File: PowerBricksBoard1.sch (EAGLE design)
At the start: 9 parts

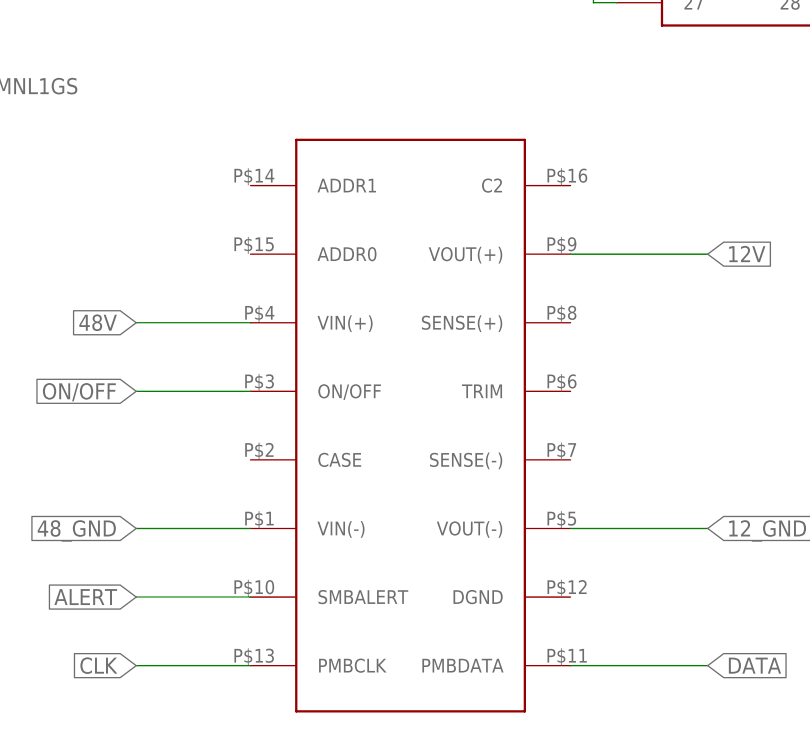
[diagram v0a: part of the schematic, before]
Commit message: updated brick part and edited connetors
had to move connector for capacitor placement
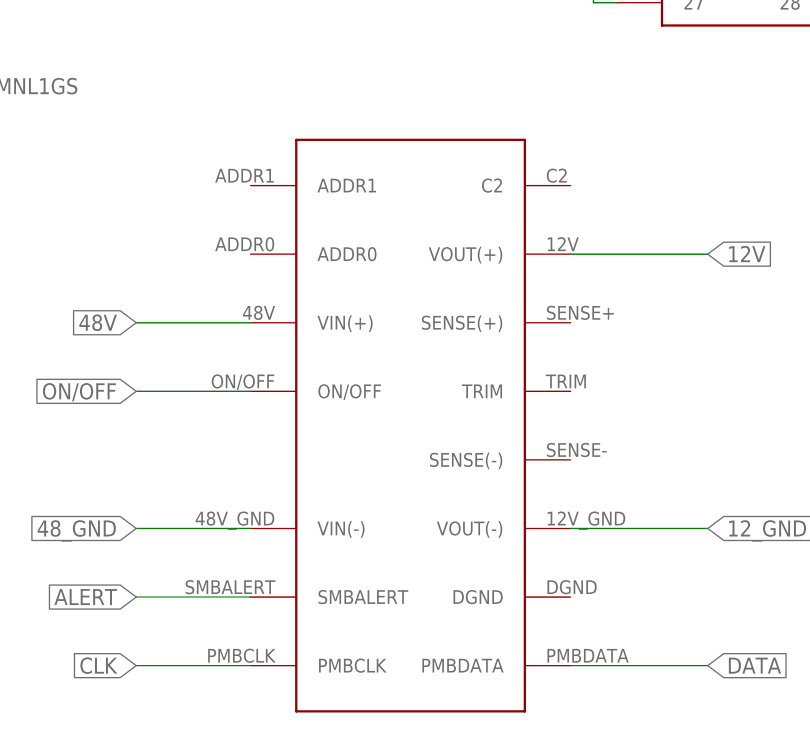
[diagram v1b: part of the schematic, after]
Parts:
- U$5: device Brickboard_Connector:BRICKBOARD_TSW_14X2 -> Dist_to_Brickboard_Connector:BRICKBOARD_TSW_14X2

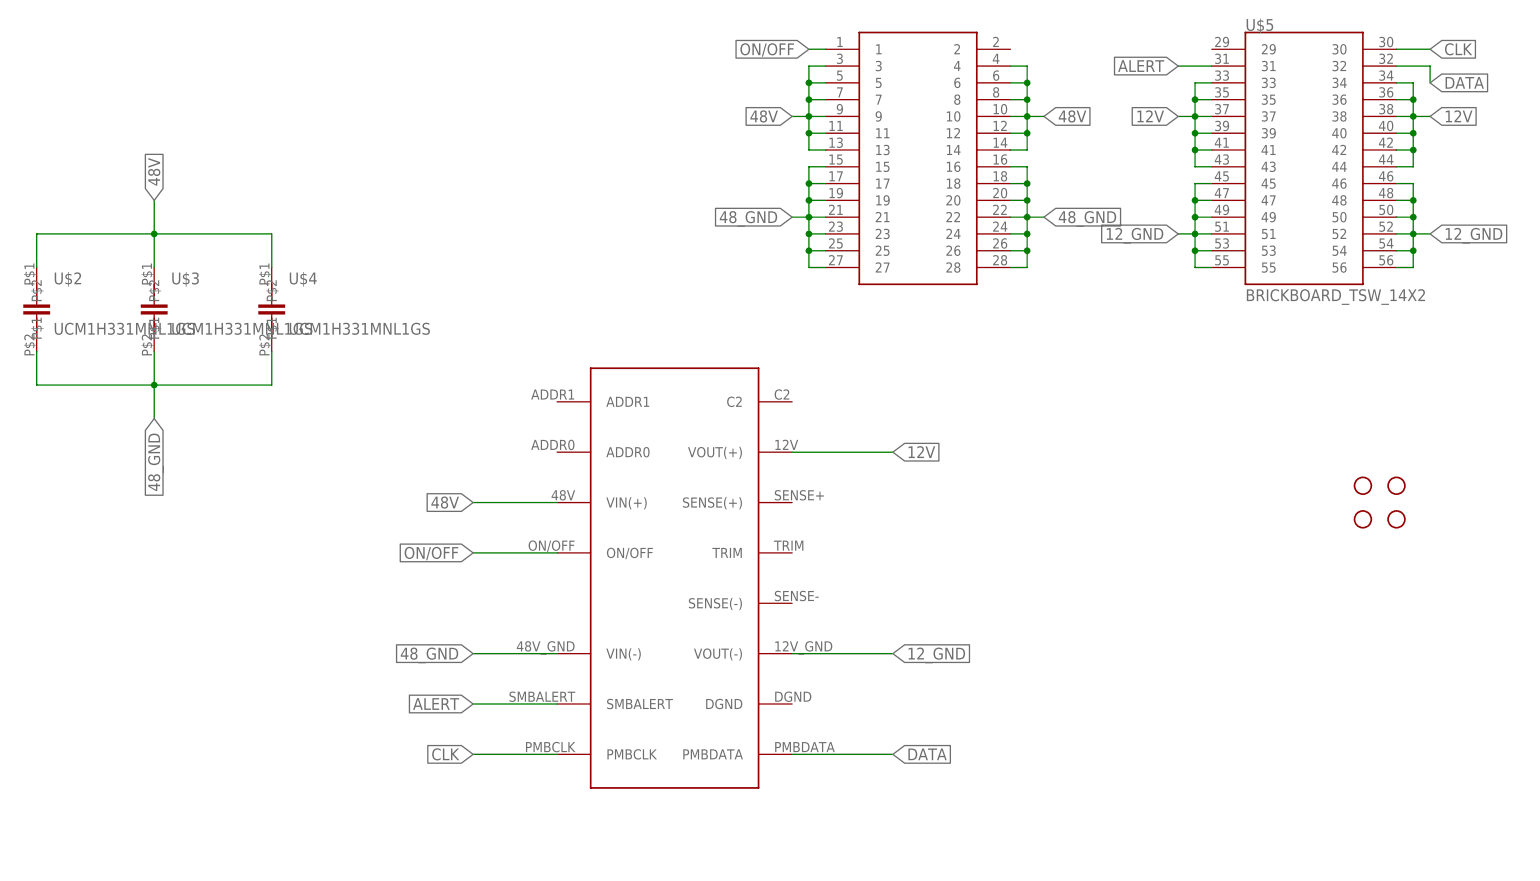
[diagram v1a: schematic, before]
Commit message: Updated Brick Board (changed connectors GND & input)
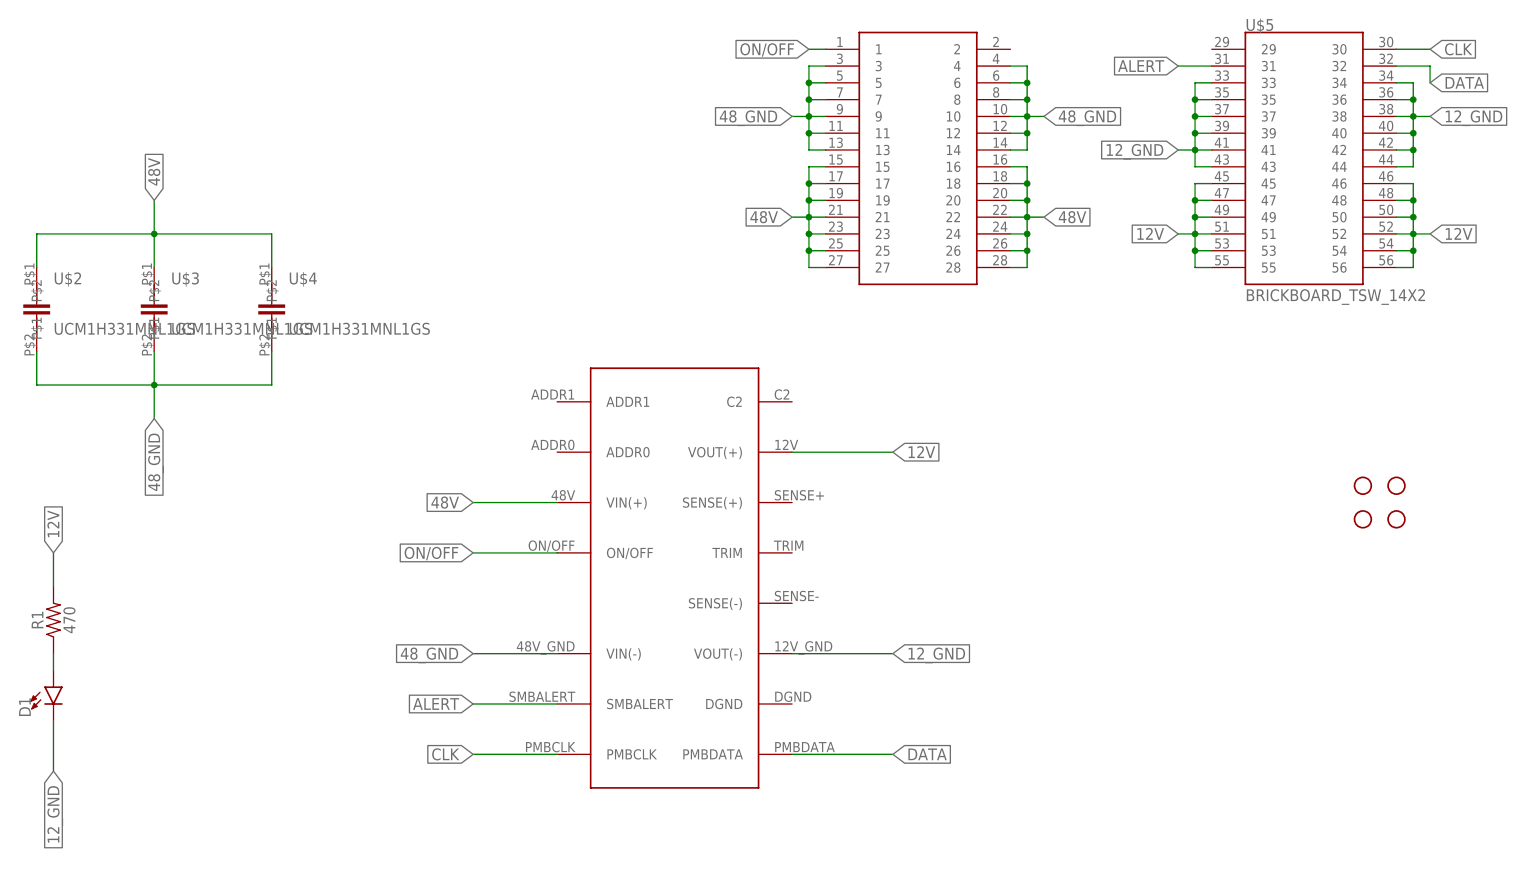
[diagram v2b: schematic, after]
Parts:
- added D1: (no value), SparkFun-LED:LED0603
- added R1: 470, SparkFun-Resistors:RESISTOR0603
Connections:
- new net N$1: D1.A, R1.1
- net 12V: now also R1.2, U$5.45, U$5.46, U$5.47, U$5.48, U$5.49, U$5.50, U$5.51, U$5.52, U$5.53, U$5.54, U$5.55, U$5.56; no longer U$5.33, U$5.34, U$5.35, U$5.36, U$5.37, U$5.38, U$5.39, U$5.40, U$5.41, U$5.42, U$5.43, U$5.44
- net 12_GND: now also D1.C, U$5.33, U$5.34, U$5.35, U$5.36, U$5.37, U$5.38, U$5.39, U$5.40, U$5.41, U$5.42, U$5.43, U$5.44; no longer U$5.45, U$5.46, U$5.47, U$5.48, U$5.49, U$5.50, U$5.51, U$5.52, U$5.53, U$5.54, U$5.55, U$5.56
- net 48V: now also U$5.15, U$5.16, U$5.17, U$5.18, U$5.19, U$5.20, U$5.21, U$5.22, U$5.23, U$5.24, U$5.25, U$5.26, U$5.27, U$5.28; no longer U$5.10, U$5.11, U$5.12, U$5.13, U$5.14, U$5.3, U$5.4, U$5.5, U$5.6, U$5.7, U$5.8, U$5.9
- net 48_GND: now also U$5.10, U$5.11, U$5.12, U$5.13, U$5.14, U$5.3, U$5.4, U$5.5, U$5.6, U$5.7, U$5.8, U$5.9; no longer U$5.15, U$5.16, U$5.17, U$5.18, U$5.19, U$5.20, U$5.21, U$5.22, U$5.23, U$5.24, U$5.25, U$5.26, U$5.27, U$5.28

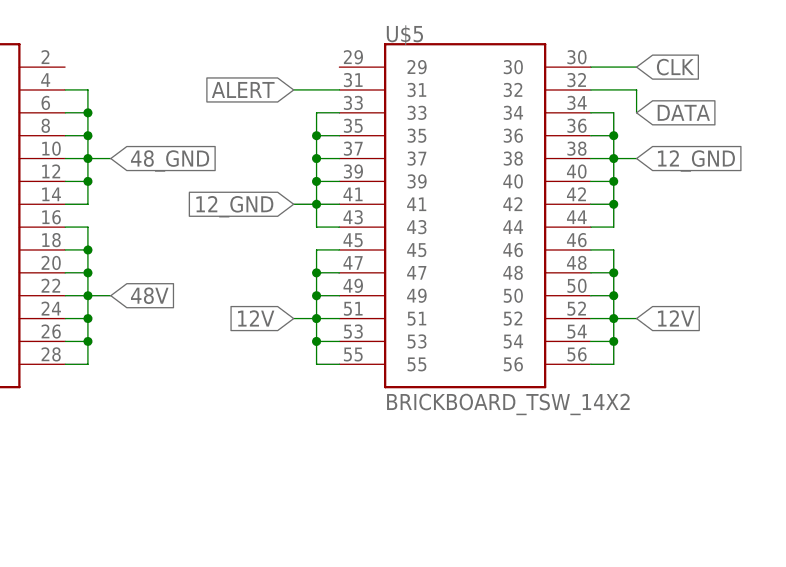
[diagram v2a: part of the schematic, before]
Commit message: updated connectors brick board (half routed)
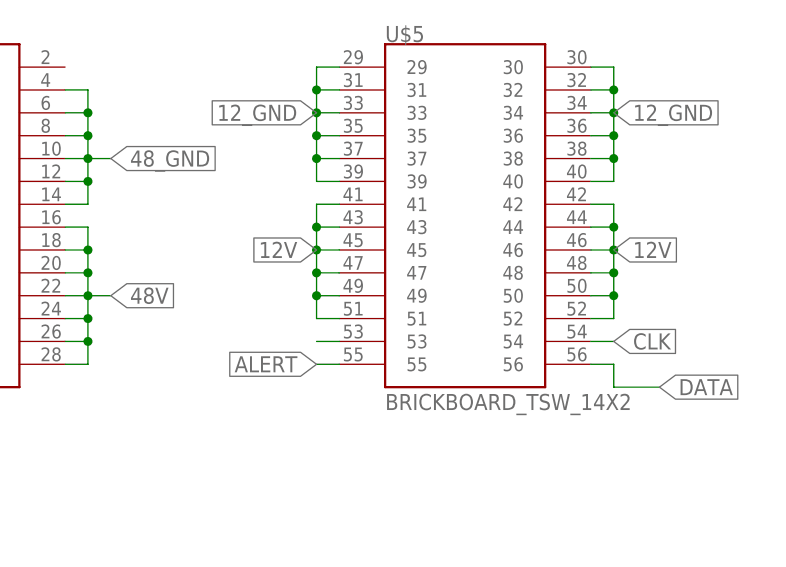
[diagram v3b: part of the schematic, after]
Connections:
- new net N$14: U$5.53
- net 12V: now also U$5.41, U$5.42, U$5.43, U$5.44; no longer U$5.53, U$5.54, U$5.55, U$5.56
- net 12_GND: now also U$5.29, U$5.30, U$5.31, U$5.32; no longer U$5.41, U$5.42, U$5.43, U$5.44
- net ALERT: now also U$5.55; no longer U$5.31
- net CLK: now also U$5.54; no longer U$5.30
- net DATA: now also U$5.56; no longer U$5.32

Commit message: Bricks updated Alumni Review
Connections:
- removed net N$14: U$5.53
- net 12V: now also U$5.53, U$5.54, U$5.55, U$5.56; no longer U$5.41, U$5.42, U$5.43, U$5.44
- net ALERT: now also U$5.43; no longer U$5.55
- net CLK: now also U$5.44; no longer U$5.54
- net DATA: now also U$5.42; no longer U$5.56
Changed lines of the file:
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@@
 </segment>
 <segment>
-<pinref part="U$5" gate="G$1" pin="41"/>
-<wire x1="81.28" y1="66.04" x2="78.74" y2="66.04" width="0.1524" layer="91"/>
-<pinref part="U$5" gate="G$1" pin="43"/>
-<wire x1="81.28" y1="63.5" x2="78.74" y2="63.5" width="0.1524" layer="91"/>
-<wire x1="78.74" y1="66.04" x2="78.74" y2="63.5" width="0.1524" layer="91"/>
+<pinref part="U$5" gate="G$1" pin="50"/>
+<wire x1="109.22" y1="55.88" x2="111.76" y2="55.88" width="0.1524" layer="91"/>
+<pinref part="U$5" gate="G$1" pin="46"/>
+<wire x1="109.22" y1="60.96" x2="111.76" y2="60.96" width="0.1524" layer="91"/>
+<pinref part="U$5" gate="G$1" pin="48"/>
+<wire x1="109.22" y1="58.42" x2="111.76" y2="58.42" width="0.1524" layer="91"/>
+<wire x1="111.76" y1="60.96" x2="111.76" y2="58.42" width="0.1524" layer="91"/>
+<wire x1="111.76" y1="55.88" x2="111.76" y2="58.42" width="0.1524" layer="91"/>
+<junction x="111.76" y="58.42"/>
+<pinref part="U$5" gate="G$1" pin="52"/>
+<wire x1="109.22" y1="53.34" x2="111.76" y2="53.34" width="0.1524" layer="91"/>
+<wire x1="111.76" y1="55.88" x2="111.76" y2="53.34" width="0.1524" layer="91"/>
+<junction x="111.76" y="55.88"/>
+<label x="111.76" y="60.96" size="1.778" layer="95" xref="yes"/>
+<wire x1="111.76" y1="53.34" x2="111.76" y2="50.8" width="0.1524" layer="91"/>
+<junction x="111.76" y="53.34"/>
+<pinref part="U$5" gate="G$1" pin="54"/>
+<wire x1="111.76" y1="50.8" x2="109.22" y2="50.8" width="0.1524" layer="91"/>
+<pinref part="U$5" gate="G$1" pin="56"/>
+<wire x1="109.22" y1="48.26" x2="111.76" y2="48.26" width="0.1524" layer="91"/>
+<wire x1="111.76" y1="50.8" x2="111.76" y2="48.26" width="0.1524" layer="91"/>
+<junction x="111.76" y="50.8"/>
+</segment>
+<segment>
+<pinref part="U$5" gate="G$1" pin="55"/>
+<wire x1="81.28" y1="48.26" x2="78.74" y2="48.26" width="0.1524" layer="91"/>
 <pinref part="U$5" gate="G$1" pin="45"/>
 <wire x1="81.28" y1="60.96" x2="78.74" y2="60.96" width="0.1524" layer="91"/>
-<wire x1="78.74" y1="63.5" x2="78.74" y2="60.96" width="0.1524" layer="91"/>
-<junction x="78.74" y="63.5"/>
 <pinref part="U$5" gate="G$1" pin="47"/>
 <wire x1="81.28" y1="58.42" x2="78.74" y2="58.42" width="0.1524" layer="91"/>
 <wire x1="78.74" y1="60.96" x2="78.74" y2="58.42" width="0.1524" layer="91"/>
-<junction x="78.74" y="60.96"/>
 <pinref part="U$5" gate="G$1" pin="49"/>
 <wire x1="81.28" y1="55.88" x2="78.74" y2="55.88" width="0.1524" layer="91"/>
@@
 <junction x="78.74" y="55.88"/>
 <label x="78.74" y="60.96" size="1.778" layer="95" rot="R180" xref="yes"/>
-</segment>
-<segment>
-<pinref part="U$5" gate="G$1" pin="50"/>
-<wire x1="109.22" y1="55.88" x2="111.76" y2="55.88" width="0.1524" layer="91"/>
-<pinref part="U$5" gate="G$1" pin="42"/>
-<wire x1="109.22" y1="66.04" x2="111.76" y2="66.04" width="0.1524" layer="91"/>
-<pinref part="U$5" gate="G$1" pin="44"/>
-<wire x1="109.22" y1="63.5" x2="111.76" y2="63.5" width="0.1524" layer="91"/>
-<wire x1="111.76" y1="66.04" x2="111.76" y2="63.5" width="0.1524" layer="91"/>
-<pinref part="U$5" gate="G$1" pin="46"/>
-<wire x1="109.22" y1="60.96" x2="111.76" y2="60.96" width="0.1524" layer="91"/>
-<wire x1="111.76" y1="63.5" x2="111.76" y2="60.96" width="0.1524" layer="91"/>
-<junction x="111.76" y="63.5"/>
-<pinref part="U$5" gate="G$1" pin="48"/>
-<wire x1="109.22" y1="58.42" x2="111.76" y2="58.42" width="0.1524" layer="91"/>
-<wire x1="111.76" y1="60.96" x2="111.76" y2="58.42" width="0.1524" layer="91"/>
-<junction x="111.76" y="60.96"/>
-<wire x1="111.76" y1="55.88" x2="111.76" y2="58.42" width="0.1524" layer="91"/>
-<junction x="111.76" y="58.42"/>
-<pinref part="U$5" gate="G$1" pin="52"/>
-<wire x1="109.22" y1="53.34" x2="111.76" y2="53.34" width="0.1524" layer="91"/>
-<wire x1="111.76" y1="55.88" x2="111.76" y2="53.34" width="0.1524" layer="91"/>
-<junction x="111.76" y="55.88"/>
-<label x="111.76" y="60.96" size="1.778" layer="95" xref="yes"/>
+<pinref part="U$5" gate="G$1" pin="53"/>
+<wire x1="81.28" y1="50.8" x2="78.74" y2="50.8" width="0.1524" layer="91"/>
+<wire x1="78.74" y1="53.34" x2="78.74" y2="50.8" width="0.1524" layer="91"/>
+<junction x="78.74" y="53.34"/>
+<wire x1="78.74" y1="50.8" x2="78.74" y2="48.26" width="0.1524" layer="91"/>
+<junction x="78.74" y="50.8"/>
 </segment>
 </net>
@@
 </segment>
 <segment>
-<pinref part="U$5" gate="G$1" pin="55"/>
-<wire x1="81.28" y1="48.26" x2="78.74" y2="48.26" width="0.1524" layer="91"/>
-<label x="78.74" y="48.26" size="1.778" layer="95" rot="R180" xref="yes"/>
+<pinref part="U$5" gate="G$1" pin="43"/>
+<wire x1="81.28" y1="63.5" x2="78.74" y2="63.5" width="0.1524" layer="91"/>
+<label x="78.74" y="63.5" size="1.778" layer="95" rot="R180" xref="yes"/>
 </segment>
 </net>
@@
 </segment>
 <segment>
-<pinref part="U$5" gate="G$1" pin="56"/>
-<wire x1="109.22" y1="48.26" x2="111.76" y2="48.26" width="0.1524" layer="91"/>
-<wire x1="111.76" y1="45.72" x2="111.76" y2="48.26" width="0.1524" layer="91"/>
-<wire x1="111.76" y1="45.72" x2="116.84" y2="45.72" width="0.1524" layer="91"/>
-<label x="116.84" y="45.72" size="1.778" layer="95" xref="yes"/>
+<pinref part="U$5" gate="G$1" pin="42"/>
+<wire x1="109.22" y1="66.04" x2="111.76" y2="66.04" width="0.1524" layer="91"/>
+<label x="111.76" y="66.04" size="1.778" layer="95" xref="yes"/>
 </segment>
 </net>
@@
 </segment>
 <segment>
-<pinref part="U$5" gate="G$1" pin="54"/>
-<wire x1="109.22" y1="50.8" x2="111.76" y2="50.8" width="0.1524" layer="91"/>
-<label x="111.76" y="50.8" size="1.778" layer="95" xref="yes"/>
+<pinref part="U$5" gate="G$1" pin="44"/>
+<wire x1="109.22" y1="63.5" x2="111.76" y2="63.5" width="0.1524" layer="91"/>
+<label x="111.76" y="63.5" size="1.778" layer="95" xref="yes"/>
 </segment>
 </net>
@@
 </segment>
 </net>
-<net name="N$14" class="0">
-<segment>
-<pinref part="U$5" gate="G$1" pin="53"/>
-<wire x1="81.28" y1="50.8" x2="78.74" y2="50.8" width="0.1524" layer="91"/>
-</segment>
-</net>
 </nets>
 </sheet>
 </sheets>
+<errors>
+</errors>
 </schematic>
 </drawing>
